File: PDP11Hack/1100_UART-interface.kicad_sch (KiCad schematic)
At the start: 24 parts, among them J3 DE9_Socket, U1 74HCT04, U1100_1 74LS126, U1100_2 74HCT02, U1100_3 74HCT02, U11_01 74LS126, U11_17 74HCT00, U3 6402, U5 74LS133, U6 74HCT00, U7 74HCT138, U8 MAX232, X1 ACO-1.1834MHz

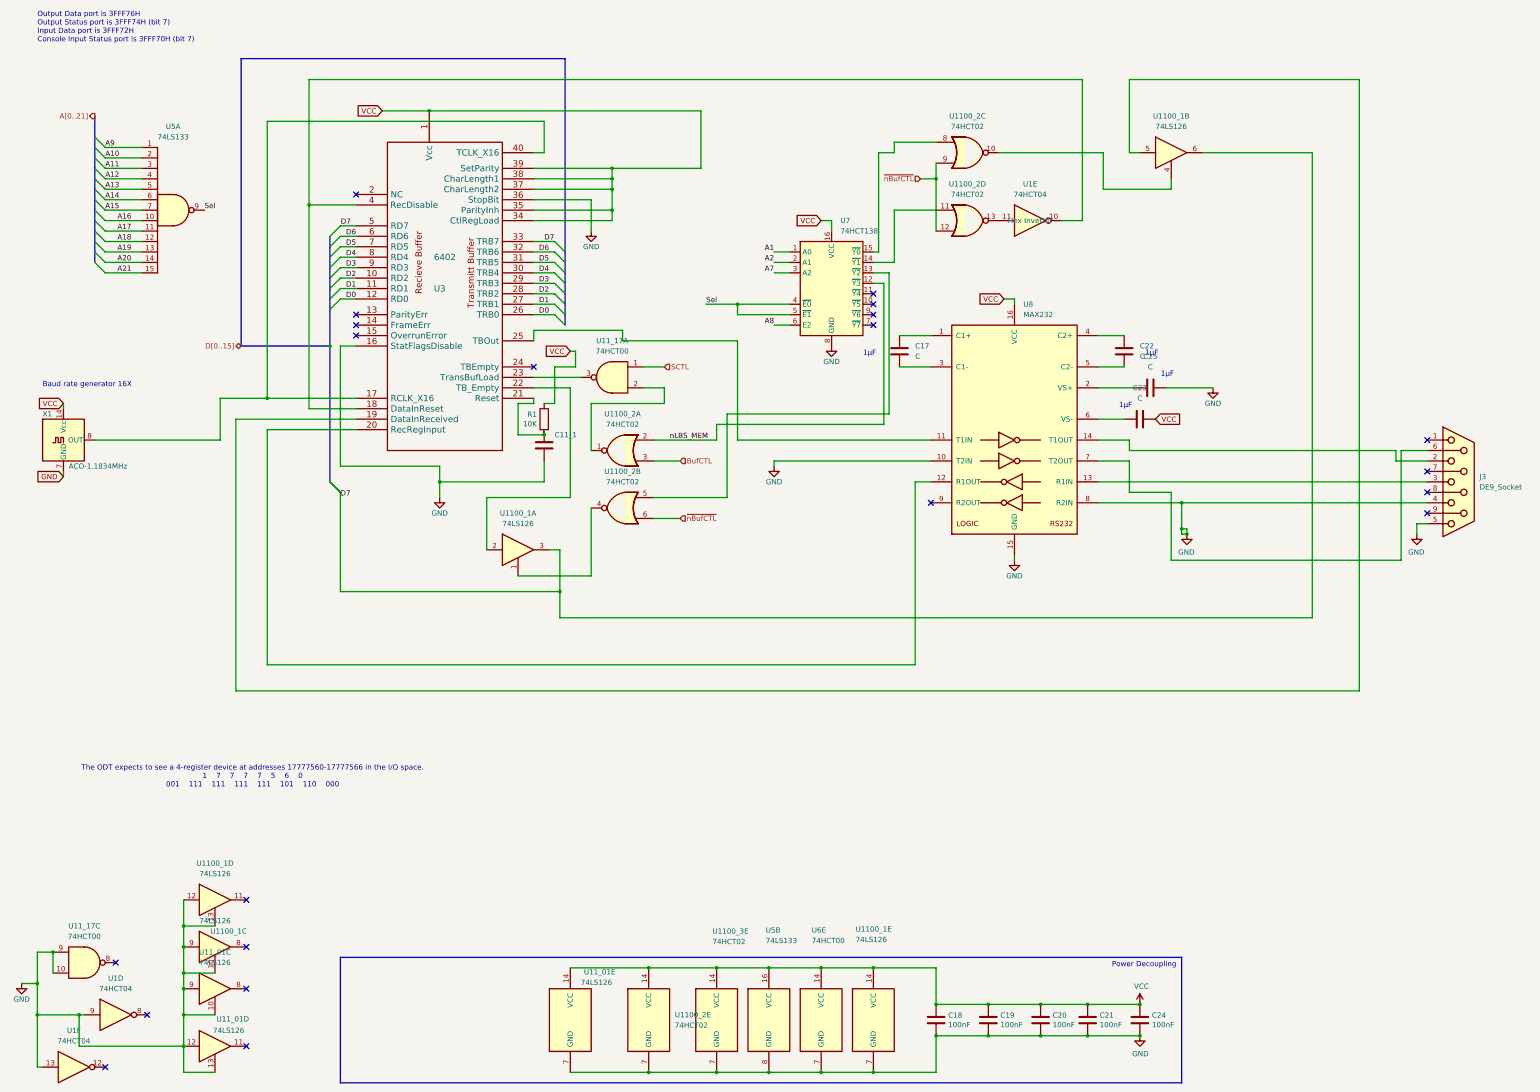
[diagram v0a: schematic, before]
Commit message: Corrections thanks to Peter Schranz on VCFED
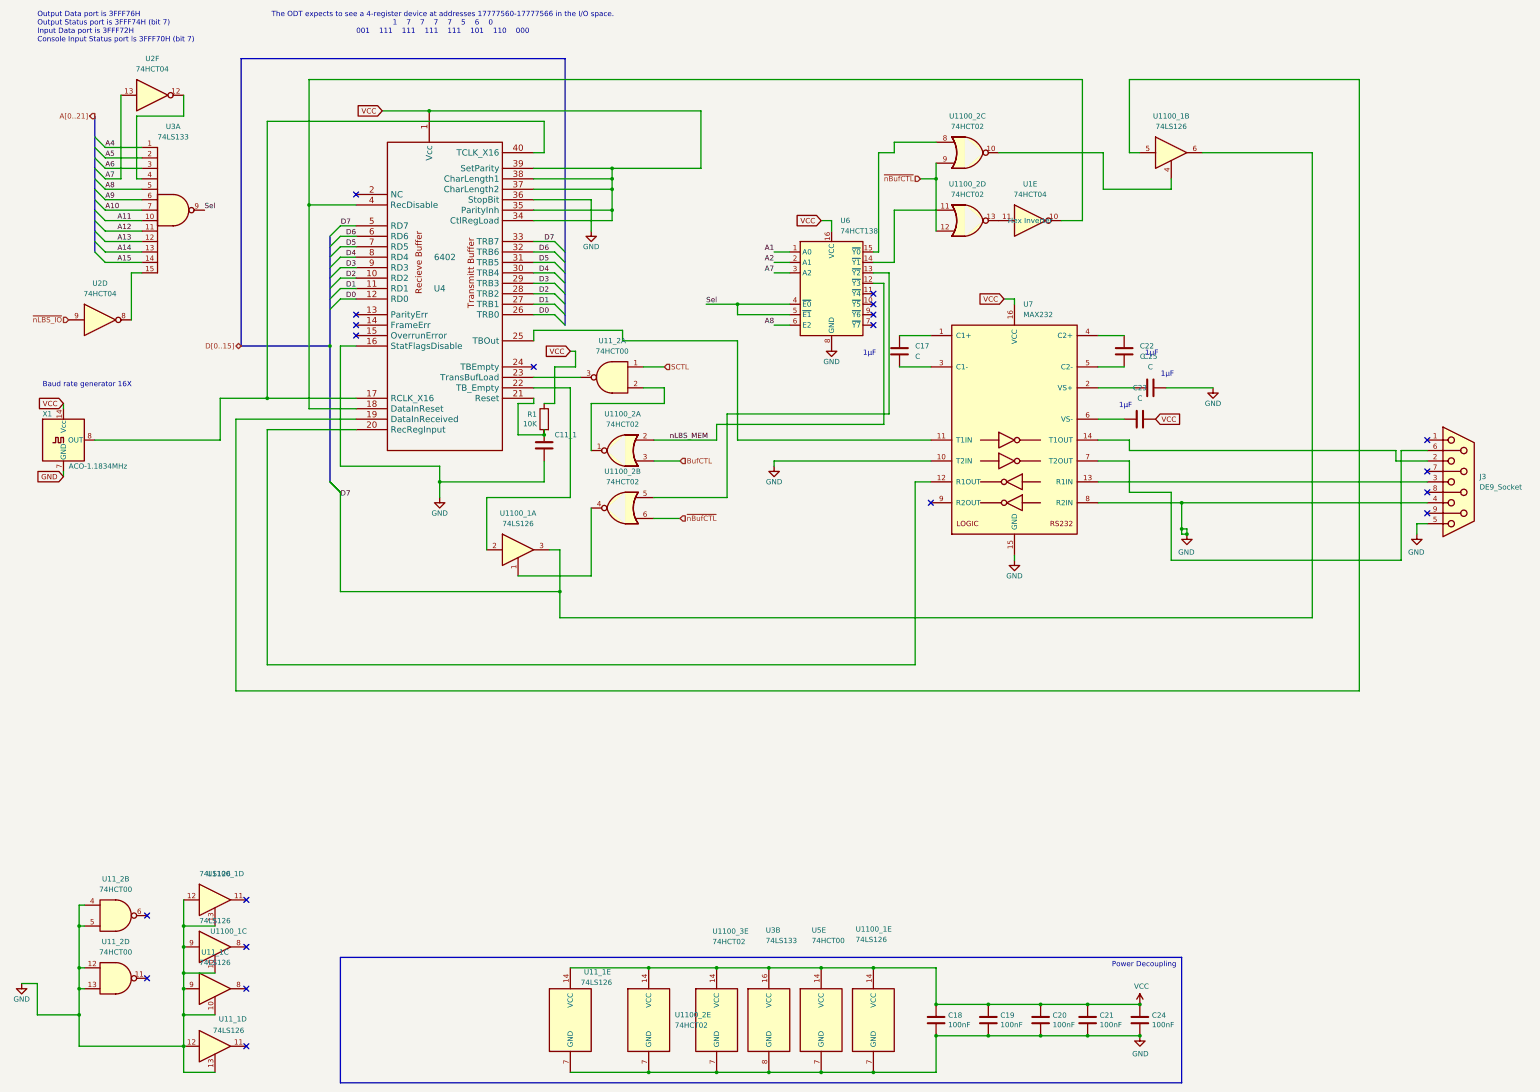
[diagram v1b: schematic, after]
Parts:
- removed unit 6 of U1
- removed unit 4 of U1
- removed unit 3 of U11_17
- added unit 4 of U11_2
- added unit 2 of U11_2
- added U2: 74HCT04, symbol 74xx:74HCT04
- renumbered U11_01 to U11_1, U11_17 to U11_2, U5 to U3, U3 to U4, U6 to U5, U7 to U6, U8 to U7
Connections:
- net A16 is gone; now on net A11: U3.10
- net A17 is gone; now on net A12: U3.11
- net A18 is gone; now on net A13: U3.12
- net A19 is gone; now on net A14: U3.13
- net A20 is gone; now on net A15: U3.14
- net A10: now also U3.7; no longer U3.2
- net A11: no longer U3.3
- net A12: no longer U3.4
- net A13: no longer U3.5
- net A14: no longer U3.6
- net A15: no longer U3.7
- net A7: now also U2.13
- net A8: now also U3.5
- net A9: now also U3.6; no longer U3.1
- net GND: now also U11_2.12, U11_2.13, U11_2.4, U11_2.5
- net A21: no longer names the net of U3.15
- net A21: now also U2.8
- new net: U2.12, U3.4
- new net A4: U3.1
- new net A5: U3.2
- new net A6: U3.3
- new net ~{nLBS_IO}: U2.9
- no-connect marks 21 -> 20

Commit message: Last update, PCB creation ready
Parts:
- removed U1100_3: 74HCT02, symbol 74xx:74HCT02
- removed U11_1: 74LS126, symbol 74xx:74LS126
- removed U5: 74HCT00, symbol 74xx:74HCT00
- C11_1: footprint Alius_6502:CP_Radial_D6.3mm_P2.50mm -> Capacitor_THT:C_Axial_L3.8mm_D2.6mm_P10.00mm_Horizontal
- C17, C22, C23, C25: footprint (none) -> Capacitor_THT:C_Axial_L3.8mm_D2.6mm_P10.00mm_Horizontal
- J3: footprint (none) -> Connector_Dsub:DSUB-9_Socket_Horizontal_P2.77x2.54mm_EdgePinOffset9.40mm
- U1, U1100_1, U1100_2, U11_2, U2: footprint (none) -> Package_DIP:DIP-14_W7.62mm
- U3, U6, U7: footprint (none) -> Package_DIP:DIP-16_W7.62mm
- U4: footprint ~ -> Package_DIP:DIP-40_W15.24mm
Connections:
- no-connect marks 20 -> 18
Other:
- moved on the sheet: R1

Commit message: Add files via upload
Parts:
- added R11_2, R11_3, R11_4, R11_5: 100 ohm, symbol Device:R
- renumbered C11_1 to C11_?, C18 to C2, C19 to C3, C20 to C4, C21 to C5, C24 to C6, C17 to C?, C25 to C?, C23 to C?, C22 to C?, J3 to J?, U6 to U1, U4 to U1100_2, U1100_1 to U1100_3, U1100_2 to U1100_4, U1100_2 to U1100_?, U1100_1 to U1100_?, U11_2 to U11_?, U7 to U15, U11_2 to U5, U3 to U?, U2 to U?, U1 to U?, X1 to X1100_1
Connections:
- net A7: now also U?.1; no longer U?.13
- net BufCTL: now also U1100_4.12; no longer U1100_4.3
- net GND: now also U1100_?.1, U1100_?.1, U1100_?.2, U1100_?.2, U11_?.1, U11_?.1, U11_?.2, U11_?.2; no longer J?.4, U1100_?.10, U1100_?.12, U1100_?.13, U1100_?.7 (GND), U1100_?.7 (GND), U1100_?.9, U11_?.12, U11_?.13, U11_?.4, U11_?.5, U15.8 (R2IN), U?.8 (GND)
- net SCTL: now also U5.4; no longer U5.1
- net VCC: no longer U1100_?.14 (VCC), U1100_?.14 (VCC), U?.16 (VCC)
- net nLBS_MEM: now also U1100_4.11; no longer U1100_4.2
- net ~{nBufCTL}: now also U1100_4.3, U1100_4.6, U1100_4.9; no longer U1100_4.12, U1100_4.6, U1100_4.9
- net ~{nLBS_IO}: now also U?.1; no longer U?.9
- net at J?.1: now also J?.4, J?.6
- net at J?.2: now also R11_2.1; no longer U15.14 (T1OUT)
- net at J?.3: now also R11_4.1; no longer U15.13 (R1IN)
- net at U15.7 (T2OUT): now also R11_5.2; no longer J?.6
- net at J?.7: now also R11_3.1
- net at J?.8: now also R11_5.1
- net at U1100_2.23 (TransBufLoad): now also U5.6; no longer U5.3
- net at U1100_2.22 (TB_Empty): now also U1100_3.9; no longer U1100_3.2
- net at U1100_3.4: now also U1100_4.4; no longer U1100_4.10
- net at U1.15 (~{Y0}): now also U1100_4.5; no longer U1100_4.8
- net at U?.15: now also U?.2; no longer U?.8
- net at U?.4: now also U?.2; no longer U?.12
- net at U1.13 (~{Y2}): now also U1100_4.8; no longer U1100_4.5
- net at U1.14 (~{Y1}): now also U1100_4.2; no longer U1100_4.11
- net at U1100_2.18 (DataInReset), U1100_2.4 (RecDisable): now also U?.2; no longer U?.10
- net D0 renamed DAL00
- net D1 renamed DAL01
- net D2 renamed DAL02
- net D3 renamed DAL03
- net D4 renamed DAL04
- net D5 renamed DAL05
- net D6 renamed DAL06
- net D7 renamed DAL07
- net DAL07: now also U1100_3.8; no longer U1100_3.3
- new net: R11_2.2, U15.14 (T1OUT)
- new net: U1100_4.13, U5.5
- new net: U1100_3.10, U1100_4.10
- new net: R11_4.2, U15.8 (R2IN)
- new net: U1100_4.1, U?.1
- new net: R11_3.2, U15.13 (R1IN)
- no-connect marks 18 -> 15
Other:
- note added: "Any and all addresses in the range (3F)E000H to (3F)FFFFH are understood to access I/O ports by the J11. When the J11 first powers up, only the address range 0H to FFFFH is available, So the decode mechanism uses only A0->A15. nLBS_IO is also used to managed the MMU/non MMU cases. Output Data port is 3FFF76H Output Status port is 3FFF74H (bit 7) Input Data port is 3FFF72H Console Input Status por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"
- note removed: "Output Data port is 3FFF76H Output Status port is 3FFF74H (bit 7) Input Data port is 3FFF72H Console Input Status port is 3FFF70H (bit 7)"
- moved on the sheet: U1100_?A

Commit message: Add files via upload
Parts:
- removed R11_2, R11_3, R11_4, R11_5: 100 ohm, symbol Device:R
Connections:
- net GND: now also J?.4, U15.8 (R2IN)
- net at J?.2: now also U15.14 (T1OUT)
- net at J?.3: now also U15.13 (R1IN)
- net at U15.7 (T2OUT): now also J?.6
- net nLBS_MEM: no longer names the net of U1.12 (~{Y3}), U1100_4.11
- now unconnected: J?.1
- no-connect marks 15 -> 18
